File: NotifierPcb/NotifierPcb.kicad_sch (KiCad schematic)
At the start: 0 parts

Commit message: done schematic
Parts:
- added C?: 0.1uF, symbol Device:C_Small
- added C?: 4.7uF, symbol Device:C_Polarized_Small
- added IC?: CD4067BEE4, DIP1080W53P254L3104H508Q24N, symbol CD4067BEE4:CD4067BEE4
- added IC?: ESP32-WROOM-32E__8MB_, ESP32WROOM32E8MB, symbol ESP32-WROOM-32E__8MB_:ESP32-WROOM-32E__8MB_
- added J?: RC_433_MHZ_RF, RC_433_RX:RC_433_RX, symbol RC_433_RX:RC_433_MHZ_RF
- added J?: Conn_01x04_Male, symbol Connector:Conn_01x04_Male
- added JP?: Enable_Jumper, symbol Jumper:Jumper_2_Open
- added JP?: Boot_Jumper, symbol Jumper:Jumper_2_Open
- added LED? (x16): PLCC2 3528, SmdLed:LEDM3528X210N, symbol PLCC2-3528:PLCC2 3528
- added R?: 100Ω, symbol Device:R_Small
- added R? (x2): 10kΩ, symbol Device:R_Small
- added U?: HT75xx-1-SOT89, Package_TO_SOT_SMD:SOT-89-3, symbol Regulator_Linear:HT75xx-1-SOT89
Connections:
- new net: LED?.1, LED?.1, LED?.1, LED?.1, LED?.1, LED?.1, LED?.1, LED?.1, LED?.1, LED?.1, LED?.1, LED?.1, LED?.1, LED?.1, LED?.1, LED?.1, R?.1
- new net +3.3V: C?.1, C?.1, IC?.1 (COMMON_OUT/IN), IC?.2 (3V3), IC?.24 (VDD), J?. (VCC), J?.2 (Pin_2), R?.1, R?.1, U?.3 (VOUT)
- new net BIT0: IC?.10 (A), IC?.7 (IO35)
- new net BIT1: IC?.11 (B), IC?.8 (IO32)
- new net BIT2: IC?.14 (C), IC?.9 (IO33)
- new net BIT3: IC?.10 (IO25), IC?.13 (D)
- new net BOOT: IC?.24 (IO2), IC?.25 (IO0), JP?.2 (B), R?.2
- new net EN: JP?.2 (B), R?.2
- new net ESP32_EN: IC?.3 (EN)
- new net GND: C?.2, C?.2, IC?.1 (GND_1), IC?.12 (VSS), IC?.15 (GND_2), IC?.15 (INHIBIT), IC?.38 (GND_3), IC?.39 (GND_4), IC?.40 (GND_5), IC?.41 (GND_6), IC?.42 (GND_7), IC?.43 (GND_8), IC?.44 (GND_9), IC?.45 (GND_10), IC?.46 (GND_11), IC?.47 (GND_12), J?. (VCC), J?.1 (Pin_1), JP?.1 (A), JP?.1 (A), R?.2, U?.1 (GND)
- new net LED0: IC?.9 (CHANNEL_IN/OUT_0), LED?.2
- new net LED1: IC?.8 (CHANNEL_IN/OUT_1), LED?.2
- new net LED10: IC?.21 (CHANNEL_IN/OUT_10), LED?.2
- new net LED11: IC?.20 (CHANNEL_IN/OUT_11), LED?.2
- new net LED12: IC?.19 (CHANNEL_IN/OUT_12), LED?.2
- new net LED13: IC?.18 (CHANNEL_IN/OUT_13), LED?.2
- new net LED14: IC?.17 (CHANNEL_IN/OUT_14), LED?.2
- new net LED15: IC?.16 (CHANNEL_IN/OUT_15), LED?.2
- new net LED2: IC?.7 (CHANNEL_IN/OUT_2), LED?.2
- new net LED3: IC?.6 (CHANNEL_IN/OUT_3), LED?.2
- new net LED4: IC?.5 (CHANNEL_IN/OUT_4), LED?.2
- new net LED5: IC?.4 (CHANNEL_IN/OUT_5), LED?.2
- new net LED6: IC?.3 (CHANNEL_IN/OUT_6), LED?.2
- new net LED7: IC?.2 (CHANNEL_IN/OUT_7), LED?.2
- new net LED8: IC?.23 (CHANNEL_IN/OUT_8), LED?.2
- new net LED9: IC?.22 (CHANNEL_IN/OUT_9), LED?.2
- new net POWER: U?.2 (VIN)
- new net RX: IC?.30 (IO18), J?. (VCC)
- new net UART_RX: IC?.34 (RXD0), J?.3 (Pin_3)
- new net UART_TX: IC?.35 (TXD0), J?.4 (Pin_4)

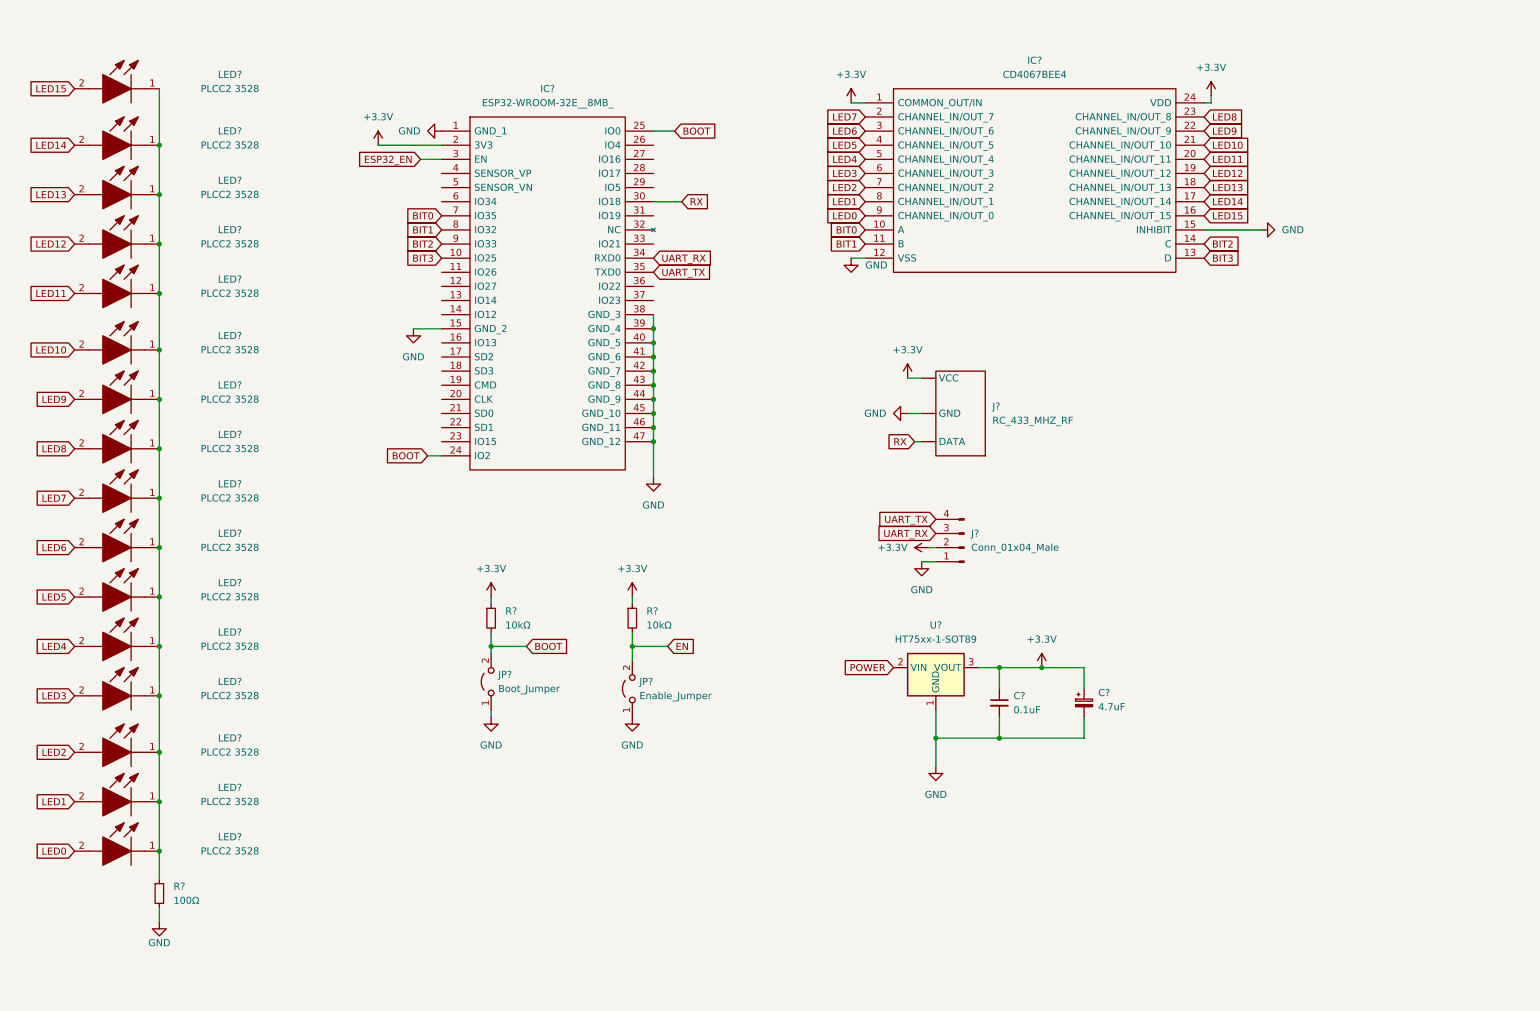
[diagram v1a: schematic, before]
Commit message: label table areas
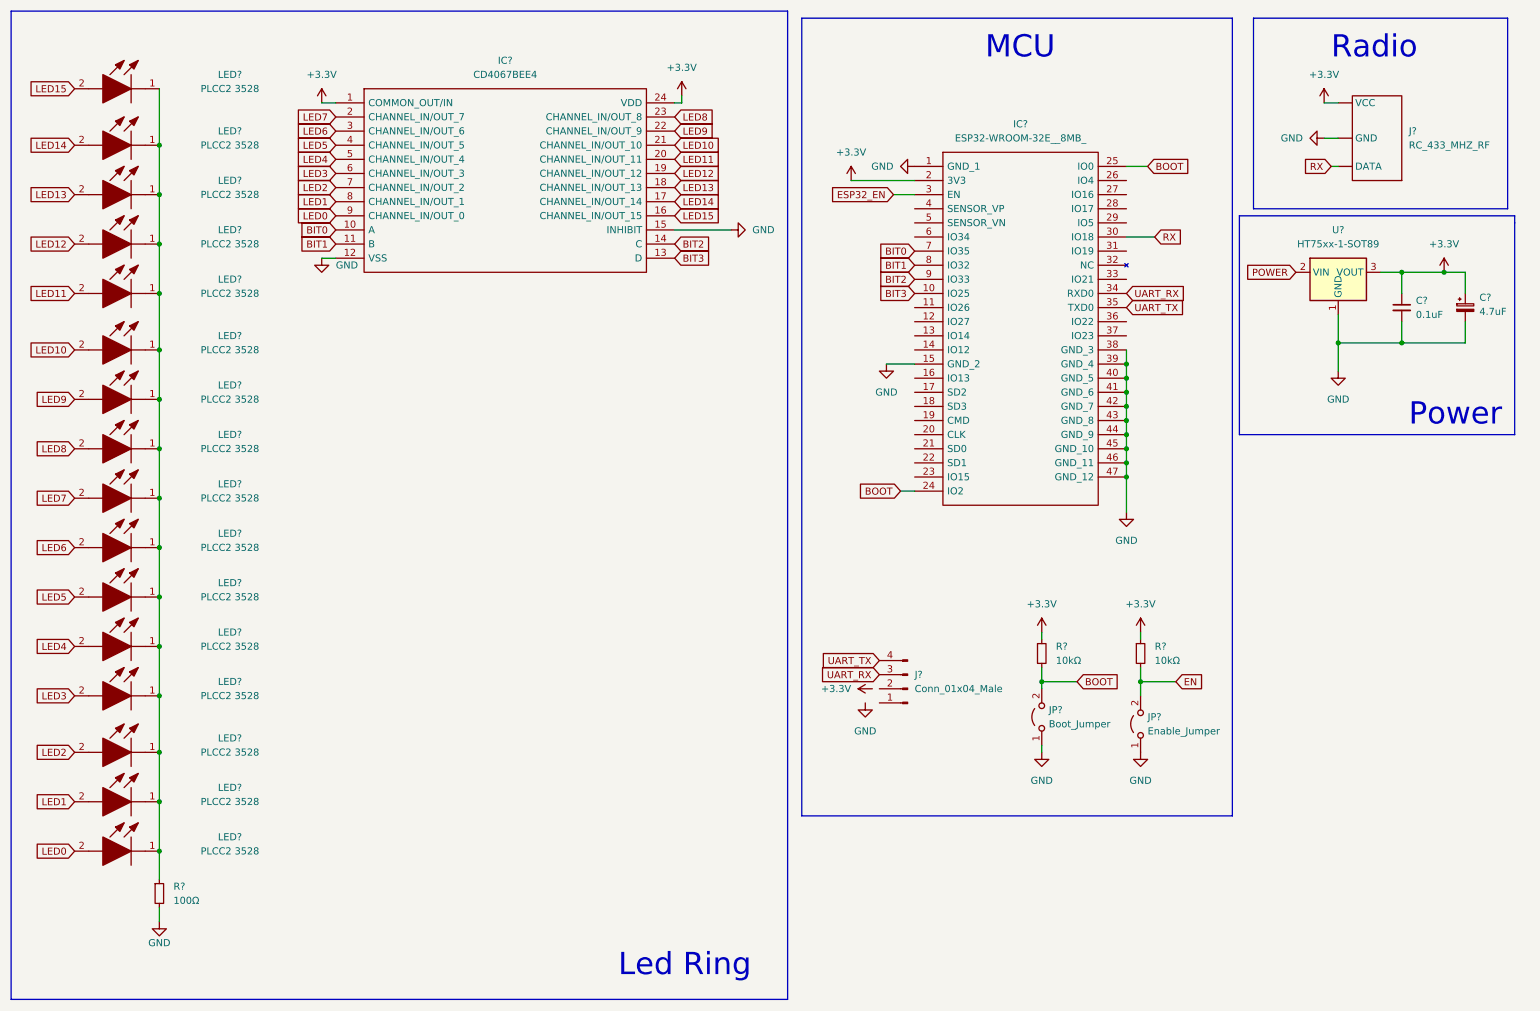
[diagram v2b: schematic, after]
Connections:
- net +3.3V: no longer J?.2 (Pin_2)
- net GND: no longer J?.1 (Pin_1)
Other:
- note added: "Led Ring"
- note added: "MCU"
- note added: "Power"
- note added: "Radio"
- moved on the sheet: C?, IC?, J?, JP?, R?, U?

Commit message: add annotations
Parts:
- gave numbers to parts that had none: 28

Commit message: wokring on pcb
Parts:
- added J?: Conn_01x02_Male, symbol Connector:Conn_01x02_Male
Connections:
- net GND: now also J?.1 (Pin_1)
- net POWER: now also J?.2 (Pin_2)
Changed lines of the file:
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@@
     (stroke (width 0) (type default) (color 0 0 0 0))
   )
-  (polyline (pts (xy 283.21 93.98) (xy 233.68 93.98))
+  (polyline (pts (xy 283.21 102.87) (xy 233.68 102.87))
+    (stroke (width 0) (type default) (color 0 0 0 0))
+  )
+  (polyline (pts (xy 233.68 93.98) (xy 233.68 102.87))
     (stroke (width 0) (type default) (color 0 0 0 0))
   )
@@
     (stroke (width 0) (type default) (color 0 0 0 0))
   )
+  (polyline (pts (xy 283.21 93.98) (xy 283.21 102.87))
+    (stroke (width 0) (type default) (color 0 0 0 0))
+  )
   (wire (pts (xy 39.37 87.63) (xy 39.37 96.52))
     (stroke (width 0) (type default) (color 0 0 0 0))
@@
     (stroke (width 0) (type default) (color 0 0 0 0))
   )
-  (text "Power" (at 264.16 92.71 0)
+  (text "Power" (at 264.16 102.87 0)
     (effects (font (size 4 4)) (justify left bottom))
   )
@@
     (property "Intersheet References" "${INTERSHEET_REFS}" (id 0) (at 140.3593 51.9906 0)
       (effects (font (size 1.27 1.27)) (justify left) hide)
+    )
+  )
+  (global_label "POWER" (shape input) (at 257.81 91.44 180) (fields_autoplaced)
+    (effects (font (size 1.27 1.27)) (justify right))
+    (property "Intersheet References" "${INTERSHEET_REFS}" (id 0) (at 248.9259 91.3606 0)
+      (effects (font (size 1.27 1.27)) (justify right) hide)
     )
   )
@@
     (pin "1")
   )
+  (symbol (lib_id "power:GND") (at 257.81 93.98 0) (unit 1)
+    (in_bom yes) (on_board yes) (fields_autoplaced)
+    (property "Reference" "#PWR?" (id 0) (at 257.81 100.33 0)
+      (effects (font (size 1.27 1.27)) hide)
+    )
+    (property "Value" "GND" (id 1) (at 257.81 99.06 0))
+    (property "Footprint" "" (id 2) (at 257.81 93.98 0)
+      (effects (font (size 1.27 1.27)) hide)
+    )
+    (property "Datasheet" "" (id 3) (at 257.81 93.98 0)
+      (effects (font (size 1.27 1.27)) hide)
+    )
+    (pin "1")
+  )
   (symbol (lib_id "PLCC2-3528:PLCC2 3528") (at 39.37 41.91 0) (mirror y) (unit 1)
     (in_bom yes) (on_board yes)
@@
     (pin "2")
   )
+  (symbol (lib_id "Connector:Conn_01x02_Male") (at 262.89 93.98 180) (unit 1)
+    (in_bom yes) (on_board yes) (fields_autoplaced)
+    (property "Reference" "J?" (id 0) (at 264.16 91.4399 0)
+      (effects (font (size 1.27 1.27)) (justify right))
+    )
+    (property "Value" "Conn_01x02_Male" (id 1) (at 264.16 93.9799 0)
+      (effects (font (size 1.27 1.27)) (justify right))
+    )
+    (property "Footprint" "" (id 2) (at 262.89 93.98 0)
+      (effects (font (size 1.27 1.27)) hide)
+    )
+    (property "Datasheet" "~" (id 3) (at 262.89 93.98 0)
+      (effects (font (size 1.27 1.27)) hide)
+    )
+    (pin "1")
+    (pin "2")
+  )
   (symbol (lib_id "power:+3.3V") (at 163.83 48.26 0) (unit 1)
     (in_bom yes) (on_board yes) (fields_autoplaced)
@@
       (reference "#PWR019") (unit 1) (value "GND") (footprint "")
     )
+    (path "/bfaf896b-f815-43d1-be7c-77e624ca03d4"
+      (reference "#PWR?") (unit 1) (value "GND") (footprint "")
+    )
     (path "/36e34b7d-0786-44b4-832b-9944d0f666aa"
       (reference "C1") (unit 1) (value "0.1uF") (footprint "")
@@
       (reference "J2") (unit 1) (value "Conn_01x04_Male") (footprint "")
     )
+    (path "/fb8a6d09-2fb4-4eda-87e1-d9aec89c042d"
+      (reference "J?") (unit 1) (value "Conn_01x02_Male") (footprint "")
+    )
     (path "/577acb1d-83fd-4af1-b1b9-3e6ce896f18a"

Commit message: arrange leds in circle, add missing components
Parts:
- C1: footprint (none) -> Capacitor_THT:C_Disc_D5.0mm_W2.5mm_P2.50mm
- C2: footprint (none) -> Capacitor_THT:CP_Radial_D8.0mm_P5.00mm
- IC1: footprint DIP1080W53P254L3104H508Q24N -> (none)
- IC2: footprint ESP32WROOM32E8MB -> (none)
- J2: footprint (none) -> Connector_PinHeader_2.54mm:PinHeader_1x04_P2.54mm_Vertical
- J3: renamed from J?; footprint (none) -> Connector_PinHeader_2.54mm:PinHeader_1x02_P2.54mm_Vertical
- JP1, JP2: footprint (none) -> Connector_PinHeader_2.54mm:PinHeader_1x02_P2.54mm_Vertical
- R1, R2, R3: footprint (none) -> Resistor_THT:R_Axial_DIN0204_L3.6mm_D1.6mm_P2.54mm_Vertical
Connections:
- net +3.3V: now also J1.1 (VCC); no longer J1. (VCC)
- net BIT0: now also IC2.9 (IO33); no longer IC2.7 (IO35)
- net BIT1: now also IC2.10 (IO25); no longer IC2.8 (IO32)
- net BIT2: now also IC2.8 (IO32); no longer IC2.9 (IO33)
- net BIT3: now also IC2.7 (IO35); no longer IC2.10 (IO25)
- net GND: now also J1.4 (GND); no longer J1. (VCC)
- net RX: now also J1.2 (DATA); no longer J1. (VCC)
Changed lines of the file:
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@@
     )
   )
-  (global_label "BIT1" (shape input) (at 175.26 63.5 180) (fields_autoplaced)
+  (global_label "BIT2" (shape input) (at 175.26 63.5 180) (fields_autoplaced)
     (effects (font (size 1.27 1.27)) (justify right))
     (property "Intersheet References" "${INTERSHEET_REFS}" (id 0) (at 168.795 63.4206 0)
@@
     )
   )
-  (global_label "BIT0" (shape input) (at 175.26 60.96 180) (fields_autoplaced)
+  (global_label "BIT3" (shape input) (at 175.26 60.96 180) (fields_autoplaced)
     (effects (font (size 1.27 1.27)) (justify right))
     (property "Intersheet References" "${INTERSHEET_REFS}" (id 0) (at 168.795 60.8806 0)
@@
     )
   )
-  (global_label "BIT3" (shape input) (at 175.26 68.58 180) (fields_autoplaced)
+  (global_label "BIT1" (shape input) (at 175.26 68.58 180) (fields_autoplaced)
     (effects (font (size 1.27 1.27)) (justify right))
     (property "Intersheet References" "${INTERSHEET_REFS}" (id 0) (at 168.795 68.5006 0)
@@
     )
   )
-  (global_label "BIT2" (shape input) (at 175.26 66.04 180) (fields_autoplaced)
+  (global_label "BIT0" (shape input) (at 175.26 66.04 180) (fields_autoplaced)
     (effects (font (size 1.27 1.27)) (justify right))
     (property "Intersheet References" "${INTERSHEET_REFS}" (id 0) (at 168.795 65.9606 0)
@@
       (effects (font (size 1.27 1.27)) hide)
     )
-    (pin "")
-    (pin "")
-    (pin "")
+    (pin "1")
+    (pin "2")
+    (pin "4")
   )
   (symbol (lib_id "PLCC2-3528:PLCC2 3528") (at 39.37 123.19 0) (mirror y) (unit 1)
@@
     (property "Reference" "IC1" (id 0) (at 101.6 26.67 0))
     (property "Value" "CD4067BEE4" (id 1) (at 101.6 29.21 0))
-    (property "Footprint" "DIP1080W53P254L3104H508Q24N" (id 2) (at 140.97 40.64 0)
+    (property "Footprint" "" (id 2) (at 140.97 40.64 0)
       (effects (font (size 1.27 1.27)) (justify left) hide)
     )
@@
       (effects (font (size 1.27 1.27)) (justify left))
     )
-    (property "Footprint" "" (id 2) (at 39.37 176.53 0)
+    (property "Footprint" "Resistor_THT:R_Axial_DIN0204_L3.6mm_D1.6mm_P2.54mm_Vertical" (id 2) (at 39.37 176.53 0)
       (effects (font (size 1.27 1.27)) hide)
     )
@@
       (effects (font (size 1.27 1.27)) (justify left))
     )
-    (property "Footprint" "" (id 2) (at 262.89 71.12 0)
+    (property "Footprint" "Capacitor_THT:C_Disc_D5.0mm_W2.5mm_P2.50mm" (id 2) (at 262.89 71.12 0)
       (effects (font (size 1.27 1.27)) hide)
     )
@@
       (effects (font (size 1.27 1.27)) (justify left))
     )
-    (property "Footprint" "" (id 2) (at 198.12 133.35 0)
+    (property "Footprint" "Resistor_THT:R_Axial_DIN0204_L3.6mm_D1.6mm_P2.54mm_Vertical" (id 2) (at 198.12 133.35 0)
       (effects (font (size 1.27 1.27)) hide)
     )
@@
       (effects (font (size 1.27 1.27)) (justify right))
     )
-    (property "Footprint" "" (id 2) (at 215.9 146.05 0)
+    (property "Footprint" "Connector_PinHeader_2.54mm:PinHeader_1x02_P2.54mm_Vertical" (id 2) (at 215.9 146.05 0)
       (effects (font (size 1.27 1.27)) hide)
     )
@@
       (effects (font (size 1.27 1.27)) (justify right))
     )
-    (property "Footprint" "" (id 2) (at 198.12 144.78 0)
+    (property "Footprint" "Connector_PinHeader_2.54mm:PinHeader_1x02_P2.54mm_Vertical" (id 2) (at 198.12 144.78 0)
       (effects (font (size 1.27 1.27)) hide)
     )
@@
     (property "Reference" "IC2" (id 0) (at 194.31 38.1 0))
     (property "Value" "ESP32-WROOM-32E__8MB_" (id 1) (at 194.31 40.64 0))
-    (property "Footprint" "ESP32WROOM32E8MB" (id 2) (at 227.33 55.88 0)
+    (property "Footprint" "" (id 2) (at 227.33 55.88 0)
       (effects (font (size 1.27 1.27)) (justify left) hide)
     )
@@
       (effects (font (size 1.27 1.27)) (justify left))
     )
-    (property "Footprint" "" (id 2) (at 215.9 133.35 0)
+    (property "Footprint" "Resistor_THT:R_Axial_DIN0204_L3.6mm_D1.6mm_P2.54mm_Vertical" (id 2) (at 215.9 133.35 0)
       (effects (font (size 1.27 1.27)) hide)
     )
@@
       (effects (font (size 1.27 1.27)) (justify left))
     )
-    (property "Footprint" "" (id 2) (at 274.32 71.12 0)
+    (property "Footprint" "Capacitor_THT:CP_Radial_D8.0mm_P5.00mm" (id 2) (at 274.32 71.12 0)
       (effects (font (size 1.27 1.27)) hide)
     )
@@
       (effects (font (size 1.27 1.27)) (justify right))
     )
-    (property "Footprint" "" (id 2) (at 173.99 139.7 0)
+    (property "Footprint" "Connector_PinHeader_2.54mm:PinHeader_1x04_P2.54mm_Vertical" (id 2) (at 173.99 139.7 0)
       (effects (font (size 1.27 1.27)) hide)
     )
@@
   (symbol (lib_id "power:GND") (at 257.81 93.98 0) (unit 1)
     (in_bom yes) (on_board yes) (fields_autoplaced)
-    (property "Reference" "#PWR?" (id 0) (at 257.81 100.33 0)
+    (property "Reference" "#PWR0101" (id 0) (at 257.81 100.33 0)
       (effects (font (size 1.27 1.27)) hide)
     )
@@
   (symbol (lib_id "Connector:Conn_01x02_Male") (at 262.89 93.98 180) (unit 1)
     (in_bom yes) (on_board yes) (fields_autoplaced)
-    (property "Reference" "J?" (id 0) (at 264.16 91.4399 0)
+    (property "Reference" "J3" (id 0) (at 264.16 91.4399 0)
       (effects (font (size 1.27 1.27)) (justify right))
     )
@@
       (effects (font (size 1.27 1.27)) (justify right))
     )
-    (property "Footprint" "" (id 2) (at 262.89 93.98 0)
+    (property "Footprint" "Connector_PinHeader_2.54mm:PinHeader_1x02_P2.54mm_Vertical" (id 2) (at 262.89 93.98 0)
       (effects (font (size 1.27 1.27)) hide)
     )
@@
     )
     (path "/bfaf896b-f815-43d1-be7c-77e624ca03d4"
-      (reference "#PWR?") (unit 1) (value "GND") (footprint "")
+      (reference "#PWR0101") (unit 1) (value "GND") (footprint "")
     )
     (path "/36e34b7d-0786-44b4-832b-9944d0f666aa"
-      (reference "C1") (unit 1) (value "0.1uF") (footprint "")
+      (reference "C1") (unit 1) (value "0.1uF") (footprint "Capacitor_THT:C_Disc_D5.0mm_W2.5mm_P2.50mm")
     )
     (path "/85303732-d45a-4adc-9450-171b30772b1e"
-      (reference "C2") (unit 1) (value "4.7uF") (footprint "")
+      (reference "C2") (unit 1) (value "4.7uF") (footprint "Capacitor_THT:CP_Radial_D8.0mm_P5.00mm")
     )
     (path "/30be67d1-c061-402a-bc4e-31243db17f33"
-      (reference "IC1") (unit 1) (value "CD4067BEE4") (footprint "DIP1080W53P254L3104H508Q24N")
+      (reference "IC1") (unit 1) (value "CD4067BEE4") (footprint "")
     )
     (path "/64bc5bde-4097-4632-869d-e864feda4607"
-      (reference "IC2") (unit 1) (value "ESP32-WROOM-32E__8MB_") (footprint "ESP32WROOM32E8MB")
+      (reference "IC2") (unit 1) (value "ESP32-WROOM-32E__8MB_") (footprint "")
     )
     (path "/2bf3865b-44eb-4f3e-8a09-39141354ac8e"
@@
     )
     (path "/b6af6992-4931-490d-9b5f-f5afe86bc848"
-      (reference "J2") (unit 1) (value "Conn_01x04_Male") (footprint "")
+      (reference "J2") (unit 1) (value "Conn_01x04_Male") (footprint "Connector_PinHeader_2.54mm:PinHeader_1x04_P2.54mm_Vertical")
     )
     (path "/fb8a6d09-2fb4-4eda-87e1-d9aec89c042d"
-      (reference "J?") (unit 1) (value "Conn_01x02_Male") (footprint "")
+      (reference "J3") (unit 1) (value "Conn_01x02_Male") (footprint "Connector_PinHeader_2.54mm:PinHeader_1x02_P2.54mm_Vertical")
     )
     (path "/577acb1d-83fd-4af1-b1b9-3e6ce896f18a"
-      (reference "JP1") (unit 1) (value "Boot_Jumper") (footprint "")
+      (reference "JP1") (unit 1) (value "Boot_Jumper") (footprint "Connector_PinHeader_2.54mm:PinHeader_1x02_P2.54mm_Vertical")
     )
     (path "/3fa373da-226e-4c94-90d8-5eae703d5a99"
-      (reference "JP2") (unit 1) (value "Enable_Jumper") (footprint "")
+      (reference "JP2") (unit 1) (value "Enable_Jumper") (footprint "Connector_PinHeader_2.54mm:PinHeader_1x02_P2.54mm_Vertical")
     )
     (path "/0768c0f5-a641-4c05-b999-29548257a079"
@@
     )
     (path "/3ddbbae6-fbbd-48e3-a894-19cd52fb19cd"
-      (reference "R1") (unit 1) (value "10kΩ") (footprint "")
+      (reference "R1") (unit 1) (value "10kΩ") (footprint "Resistor_THT:R_Axial_DIN0204_L3.6mm_D1.6mm_P2.54mm_Vertical")
     )
     (path "/68e43655-d922-46c0-9b55-f3cad6d3ac54"
-      (reference "R2") (unit 1) (value "10kΩ") (footprint "")
+      (reference "R2") (unit 1) (value "10kΩ") (footprint "Resistor_THT:R_Axial_DIN0204_L3.6mm_D1.6mm_P2.54mm_Vertical")
     )
     (path "/335853c2-eacf-46ef-a301-fa344f5c7e94"
-      (reference "R3") (unit 1) (value "100Ω") (footprint "")
+      (reference "R3") (unit 1) (value "100Ω") (footprint "Resistor_THT:R_Axial_DIN0204_L3.6mm_D1.6mm_P2.54mm_Vertical")
     )
     (path "/083982aa-79db-49d1-a0f9-5c7edbb1e88f"

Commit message: done pcb beta version
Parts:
- IC2: footprint (none) -> ESP32WROOM32E8MB
- J2: value Conn_01x04_Male -> UART_Conn
- J3: value Conn_01x02_Male -> Power_Conn
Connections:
- net EN is gone; now on net ESP32_EN: JP2.2 (B), R2.2
- net +3.3V: now also J2.2 (Pin_2)
- net GND: now also J2.1 (Pin_1)
- net RX: now also IC2.37 (IO23); no longer IC2.30 (IO18)
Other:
- moved on the sheet: JP1, JP2, R1, R2
